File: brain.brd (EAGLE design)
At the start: 100 x 80 mm, 24 parts, among them IC1 LP2950ACZ-3.3, IC2 LP2950ACZ-3.3, U1 TINY45-20-DIP, U4 TINY45-20-DIP, U5 TINY45-20-DIP, U6 TINY45-20-DIP

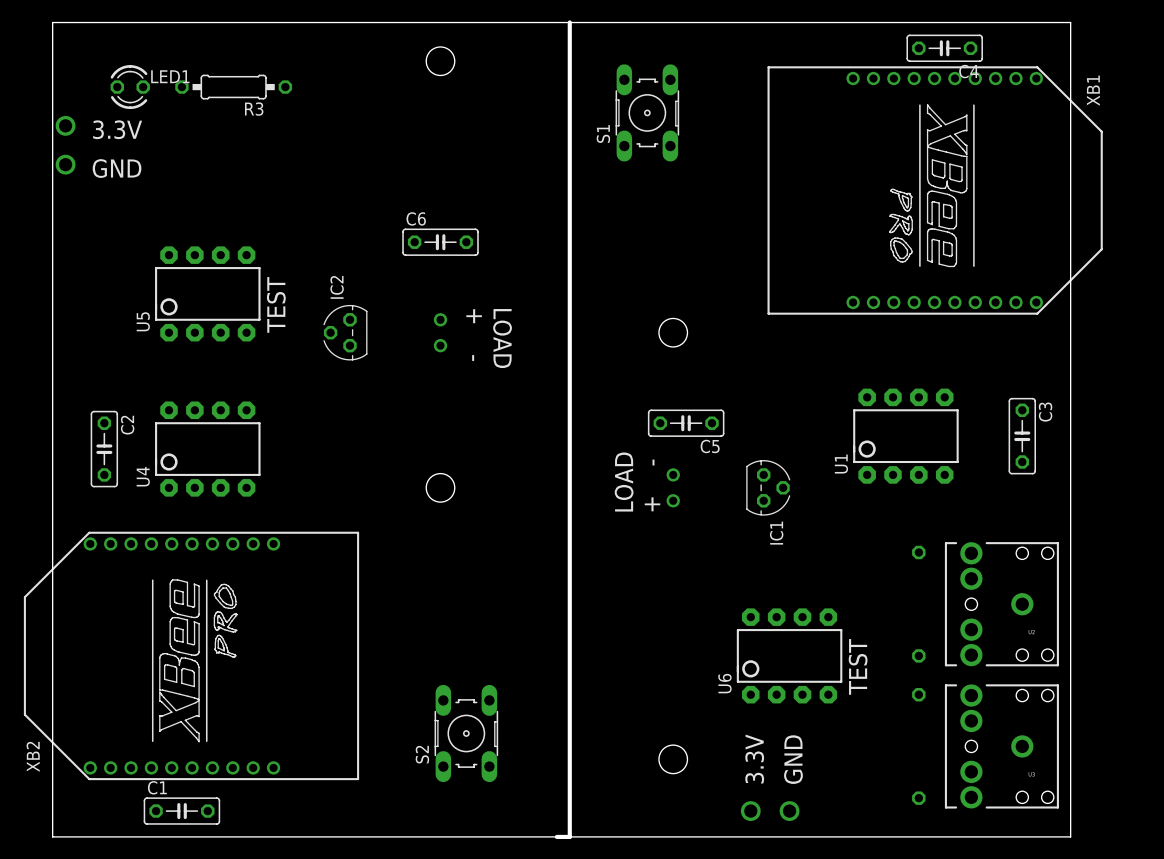
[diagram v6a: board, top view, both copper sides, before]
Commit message: uhh we probably moved something. uncertain. nothing major. tied the inputs of the 3.5mm jacks together.
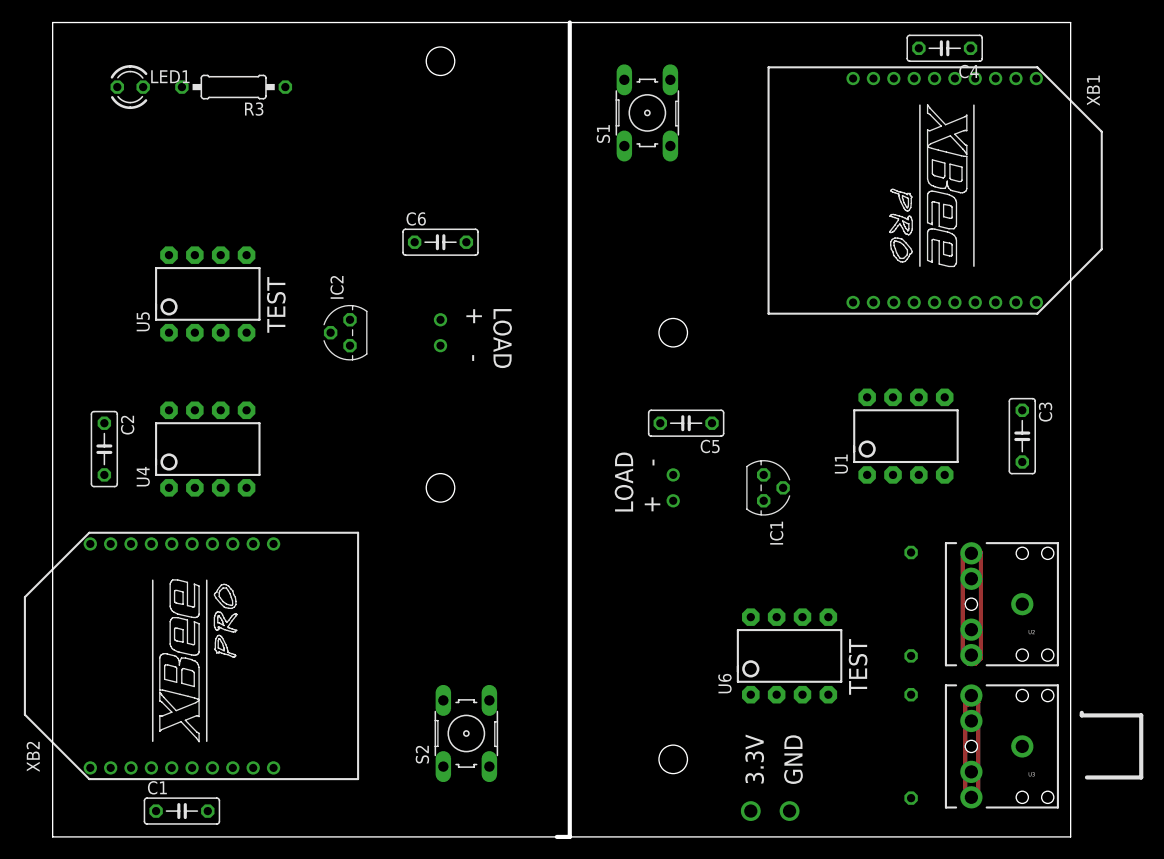
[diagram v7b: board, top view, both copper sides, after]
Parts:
- moved R1 0.76 mm to (84.3, 22.9), turned to 90 degrees
- moved R2 0.76 mm to (84.3, 8.89)
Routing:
- net N$2: track 0.00 -> 25.9 mm, vias 1 -> 0
- net N$1: track 0.00 -> 21.6 mm, vias 1 -> 0
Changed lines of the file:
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@@
 <setting verticaltext="up"/>
 </settings>
-<grid distance="0.05" unitdist="inch" unit="inch" style="dots" multiple="1" display="no" altdistance="0.025" altunitdist="inch" altunit="inch"/>
+<grid distance="0.01" unitdist="inch" unit="inch" style="dots" multiple="1" display="no" altdistance="0.025" altunitdist="inch" altunit="inch"/>
 <layers>
 <layer number="1" name="Top" color="4" fill="1" visible="yes" active="yes"/>
@@
 <layer number="100" name="Muster" color="7" fill="1" visible="no" active="no"/>
 <layer number="101" name="Patch_Top" color="12" fill="4" visible="yes" active="yes"/>
-<layer number="102" name="Vscore" color="12" fill="1" visible="yes" active="yes"/>
+<layer number="102" name="Vscore" color="32" fill="1" visible="yes" active="yes"/>
 <layer number="103" name="tMap" color="7" fill="1" visible="yes" active="yes"/>
 <layer number="104" name="Name" color="16" fill="1" visible="yes" active="yes"/>
@@
 <text x="80.01" y="13.97" size="1.778" layer="21" rot="R90">TEST</text>
 <text x="22.86" y="49.53" size="1.778" layer="21" rot="R90">TEST</text>
-<text x="3.81" y="68.58" size="1.778" layer="21">3.3V</text>
-<text x="3.81" y="64.77" size="1.778" layer="21">GND</text>
 <text x="69.85" y="5.08" size="1.778" layer="21" rot="R90">3.3V</text>
 <text x="73.66" y="5.08" size="1.778" layer="21" rot="R90">GND</text>
+<dimension x1="56.1594" y1="74.3712" x2="60.706" y2="74.422" x3="58.4327" y3="74.3966" textsize="2.54" layer="21"/>
+<dimension x1="60.6806" y1="67.8688" x2="60.706" y2="74.168" x3="61.723621875" y3="71.01424375" textsize="2.54" layer="21"/>
+<wire x1="101.6" y1="5.842" x2="106.934" y2="5.842" width="0.4064" layer="21"/>
+<wire x1="106.934" y1="5.842" x2="106.934" y2="11.938" width="0.4064" layer="21"/>
+<wire x1="106.934" y1="11.938" x2="101.092" y2="11.938" width="0.4064" layer="21"/>
+<wire x1="101.092" y1="11.938" x2="101.092" y2="12.192" width="0.4064" layer="21"/>
+<dimension x1="101.6" y1="5.842" x2="101.6" y2="11.938" x3="103.632" y3="8.89" textsize="2.54" layer="21"/>
 </plain>
 <attributes>
@@
 </autorouter>
 <elements>
-<element name="R1" library="resistor" package="0207/10" value="10k" x="85.09" y="22.86" rot="MR270">
-<attribute name="OC_NEWARK" value="64R8539" x="85.09" y="22.86" size="1.778" layer="28" rot="MR270" display="off"/>
-<attribute name="MPN" value="LT3652EMSE#PBF" x="85.09" y="22.86" size="1.778" layer="28" rot="MR270" display="off"/>
-<attribute name="MF" value="" x="85.09" y="22.86" size="1.778" layer="28" rot="MR270" display="off"/>
-</element>
-<element name="R2" library="resistor" package="0207/10" value="10k" x="85.09" y="8.89" rot="MR270">
-<attribute name="OC_NEWARK" value="64R8539" x="85.09" y="8.89" size="1.778" layer="28" rot="MR270" display="off"/>
-<attribute name="MPN" value="LT3652EMSE#PBF" x="85.09" y="8.89" size="1.778" layer="28" rot="MR270" display="off"/>
-<attribute name="MF" value="" x="85.09" y="8.89" size="1.778" layer="28" rot="MR270" display="off"/>
+<element name="R1" library="resistor" package="0207/10" value="10k" x="84.328" y="22.86" rot="MR90">
+<attribute name="OC_NEWARK" value="64R8539" x="84.328" y="22.86" size="1.778" layer="28" rot="MR90" display="off"/>
+<attribute name="MPN" value="LT3652EMSE#PBF" x="84.328" y="22.86" size="1.778" layer="28" rot="MR90" display="off"/>
+<attribute name="MF" value="" x="84.328" y="22.86" size="1.778" layer="28" rot="MR90" display="off"/>
+</element>
+<element name="R2" library="resistor" package="0207/10" value="10k" x="84.328" y="8.89" rot="MR270">
+<attribute name="OC_NEWARK" value="64R8539" x="84.328" y="8.89" size="1.778" layer="28" rot="MR270" display="off"/>
+<attribute name="MPN" value="LT3652EMSE#PBF" x="84.328" y="8.89" size="1.778" layer="28" rot="MR270" display="off"/>
+<attribute name="MF" value="" x="84.328" y="8.89" size="1.778" layer="28" rot="MR270" display="off"/>
 </element>
 <element name="S1" library="switch-omron" package="B3F-10XX" value="" x="58.42" y="71.12" rot="R90">
@@
 <contactref element="U1" pad="7"/>
 <contactref element="U6" pad="7"/>
-<wire x1="85.09" y1="27.94" x2="82.55" y2="43.18" width="0" layer="19" extent="1-1"/>
-<wire x1="90.25" y1="17.86" x2="85.09" y2="27.94" width="0" layer="19" extent="1-1"/>
-<wire x1="71.12" y1="21.59" x2="85.09" y2="27.94" width="0" layer="19" extent="1-1"/>
+<wire x1="84.328" y1="17.78" x2="82.55" y2="43.18" width="0" layer="19" extent="1-1"/>
+<wire x1="90.25" y1="17.86" x2="84.328" y2="17.78" width="0" layer="19" extent="1-1"/>
+<wire x1="71.12" y1="21.59" x2="84.328" y2="17.78" width="0" layer="19" extent="1-1"/>
 </signal>
 <signal name="N$13">
@@
 <contactref element="IC2" pad="3"/>
 <contactref element="C6" pad="1"/>
+<wire x1="38.1" y1="50.8" x2="35.56" y2="58.42" width="0" layer="19" extent="1-1"/>
 <wire x1="29.21" y1="50.8" x2="38.1" y2="50.8" width="0" layer="19" extent="1-1"/>
-<wire x1="35.56" y1="58.42" x2="29.21" y2="50.8" width="0" layer="19" extent="1-1"/>
 </signal>
 <signal name="N$8">
@@
 <wire x1="78.63" y1="74.5" x2="85.09" y2="77.47" width="0" layer="19" extent="1-1"/>
 <wire x1="56.1594" y1="74.3712" x2="78.63" y2="74.5" width="0" layer="19" extent="1-1"/>
-<wire x1="60.96" y1="35.56" x2="56.1594" y2="74.3712" width="0" layer="19" extent="1-1"/>
+<wire x1="59.69" y1="40.64" x2="56.1594" y2="74.3712" width="0" layer="19" extent="1-1"/>
+<wire x1="60.96" y1="35.56" x2="59.69" y2="40.64" width="0" layer="19" extent="1-1"/>
 <wire x1="71.755" y1="34.29" x2="60.96" y2="35.56" width="0" layer="19" extent="1-1"/>
-<wire x1="59.69" y1="40.64" x2="60.96" y2="35.56" width="0" layer="19" extent="1-1"/>
-<wire x1="85.09" y1="17.78" x2="59.69" y2="40.64" width="0" layer="19" extent="1-1"/>
-<wire x1="85.09" y1="3.81" x2="85.09" y2="17.78" width="0" layer="19" extent="1-1"/>
 <wire x1="87.63" y1="35.56" x2="71.755" y2="34.29" width="0" layer="19" extent="1-1"/>
 <wire x1="95.25" y1="36.83" x2="87.63" y2="35.56" width="0" layer="19" extent="1-1"/>
-<wire x1="76.2" y1="13.97" x2="59.69" y2="40.64" width="0" layer="19" extent="1-1"/>
+<wire x1="84.328" y1="27.94" x2="87.63" y2="35.56" width="0" layer="19" extent="1-1"/>
+<wire x1="76.2" y1="13.97" x2="84.328" y2="27.94" width="0" layer="19" extent="1-1"/>
+<wire x1="84.328" y1="3.81" x2="76.2" y2="13.97" width="0" layer="19" extent="1-1"/>
 </signal>
 <signal name="VCC1">
@@
 <contactref element="IC1" pad="3"/>
 <contactref element="C5" pad="1"/>
-<wire x1="60.96" y1="33.02" x2="69.85" y2="33.02" width="0" layer="19" extent="1-1"/>
-<wire x1="64.77" y1="40.64" x2="60.96" y2="33.02" width="0" layer="19" extent="1-1"/>
+<wire x1="60.96" y1="33.02" x2="64.77" y2="40.64" width="0" layer="19" extent="1-1"/>
+<wire x1="69.85" y1="33.02" x2="60.96" y2="33.02" width="0" layer="19" extent="1-1"/>
 </signal>
 <signal name="TX1">
@@
 <wire x1="95.25" y1="22.86" x2="87.63" y2="43.18" width="0" layer="19" extent="1-1"/>
 <wire x1="95.25" y1="8.89" x2="95.25" y2="22.86" width="0" layer="19" extent="1-1"/>
-<wire x1="76.2" y1="21.59" x2="95.25" y2="8.89" width="0" layer="19" extent="1-1"/>
+<wire x1="76.2" y1="21.59" x2="95.25" y2="22.86" width="0" layer="19" extent="1-1"/>
 </signal>
 <signal name="PB11">
@@
 <contactref element="U3" pad="RING"/>
 <contactref element="U1" pad="6"/>
-<wire x1="85.09" y1="13.97" x2="85.09" y2="43.18" width="0" layer="19" extent="1-1"/>
-<wire x1="90.25" y1="3.89" x2="85.09" y2="13.97" width="0" layer="19" extent="1-1"/>
-<wire x1="73.66" y1="21.59" x2="85.09" y2="13.97" width="0" layer="19" extent="1-1"/>
+<wire x1="73.66" y1="21.59" x2="85.09" y2="43.18" width="0" layer="19" extent="1-1"/>
+<wire x1="84.328" y1="13.97" x2="73.66" y2="21.59" width="0" layer="19" extent="1-1"/>
+<wire x1="90.25" y1="3.89" x2="84.328" y2="13.97" width="0" layer="19" extent="1-1"/>
 </signal>
 <signal name="PB51">
@@
 <wire x1="68.58" y1="13.97" x2="80.01" y2="35.56" width="0" layer="19" extent="1-1"/>
 </signal>
-<signal name="N$1">
-<via x="1.27" y="69.85" extent="1-16" drill="1.3" shape="square"/>
-</signal>
-<signal name="N$2">
-<via x="1.27" y="66.04" extent="1-16" drill="1.3" shape="square"/>
-</signal>
 <signal name="N$3">
 <via x="68.58" y="2.54" extent="1-16" drill="1.3" shape="square"/>
@@
 <via x="72.39" y="2.54" extent="1-16" drill="1.3" shape="square"/>
 </signal>
+<signal name="N$1">
+<wire x1="89.916" y1="13.208" x2="89.662" y2="13.208" width="0.4064" layer="1"/>
+<wire x1="89.662" y1="13.208" x2="89.662" y2="3.81" width="0.4064" layer="1"/>
+<wire x1="89.662" y1="3.81" x2="90.932" y2="3.81" width="0.4064" layer="1"/>
+<wire x1="90.932" y1="3.81" x2="90.932" y2="13.208" width="0.4064" layer="1"/>
+<wire x1="90.932" y1="13.208" x2="89.916" y2="13.208" width="0.4064" layer="1"/>
+<wire x1="89.916" y1="13.208" x2="89.916" y2="12.954" width="0.4064" layer="1"/>
+</signal>
+<signal name="N$2">
+<wire x1="89.408" y1="28.194" x2="89.408" y2="27.686" width="0.4064" layer="1"/>
+<wire x1="89.408" y1="27.686" x2="89.408" y2="17.526" width="0.4064" layer="1"/>
+<wire x1="89.408" y1="17.526" x2="89.916" y2="17.018" width="0.4064" layer="1"/>
+<wire x1="89.916" y1="17.018" x2="90.678" y2="17.018" width="0.4064" layer="1"/>
+<wire x1="90.678" y1="17.018" x2="91.186" y2="17.526" width="0.4064" layer="1"/>
+<wire x1="91.186" y1="17.526" x2="91.186" y2="27.94" width="0.4064" layer="1"/>
+<wire x1="91.186" y1="27.94" x2="90.678" y2="28.448" width="0.4064" layer="1"/>
+<wire x1="90.678" y1="28.448" x2="89.662" y2="28.448" width="0.4064" layer="1"/>
+<wire x1="89.662" y1="28.448" x2="89.662" y2="27.94" width="0.4064" layer="1"/>
+<wire x1="89.662" y1="27.94" x2="89.408" y2="27.686" width="0.4064" layer="1"/>
+</signal>
 </signals>

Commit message: Added routing. Looks like everything should be good. Put in via line because the $33 boards don't support scoring.
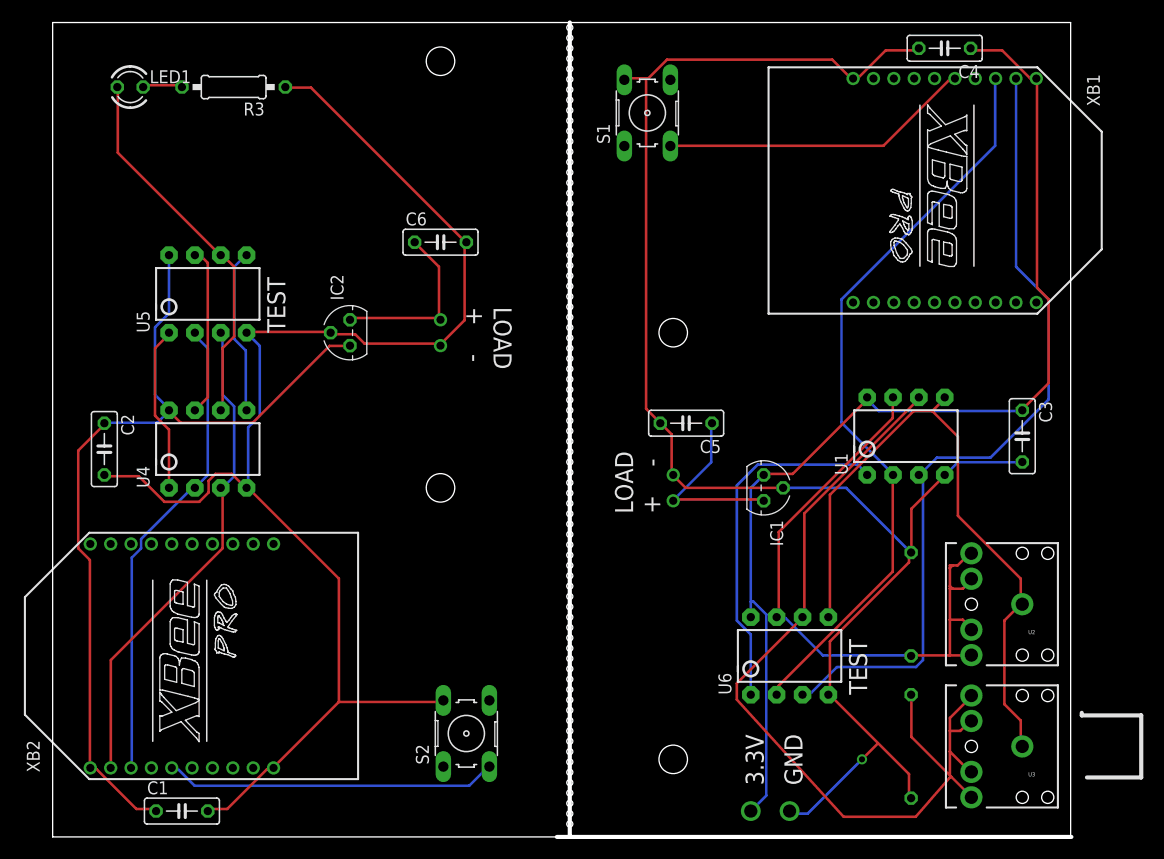
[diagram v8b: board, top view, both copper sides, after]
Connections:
- removed net N$14: U5.2
- removed net N$7: U4.7
- new net PB22: U4.7, U5.7
- net TX2: now also U5.2; no longer U5.7
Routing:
- net GND1: track 0.00 -> 146.6 mm
- net GND2: track 0.00 -> 141.4 mm
- net VCC1: track 0.00 -> 107.3 mm
- net VOUT2: track 0.00 -> 88.4 mm
- net RX1: track 0.00 -> 80.3 mm
- net PB11: track 0.00 -> 77.5 mm
- net TX1: track 0.00 -> 73.6 mm
- net PB01: track 0.00 -> 65.5 mm
- net RX2: track 0.00 -> 48.7 mm
- net PB21: track 0.00 -> 47.1 mm
- net TX2: track 0.00 -> 46.7 mm
- net PB12: track 0.00 -> 36.9 mm
- net PB51: track 0.00 -> 35.3 mm
- net N$8: track 0.00 -> 32.7 mm
- net N$13: track 0.00 -> 30.7 mm
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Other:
- board size 100 x 80 mm -> 100.1 x 80 mm
